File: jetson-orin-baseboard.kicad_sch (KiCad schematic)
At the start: 4 parts

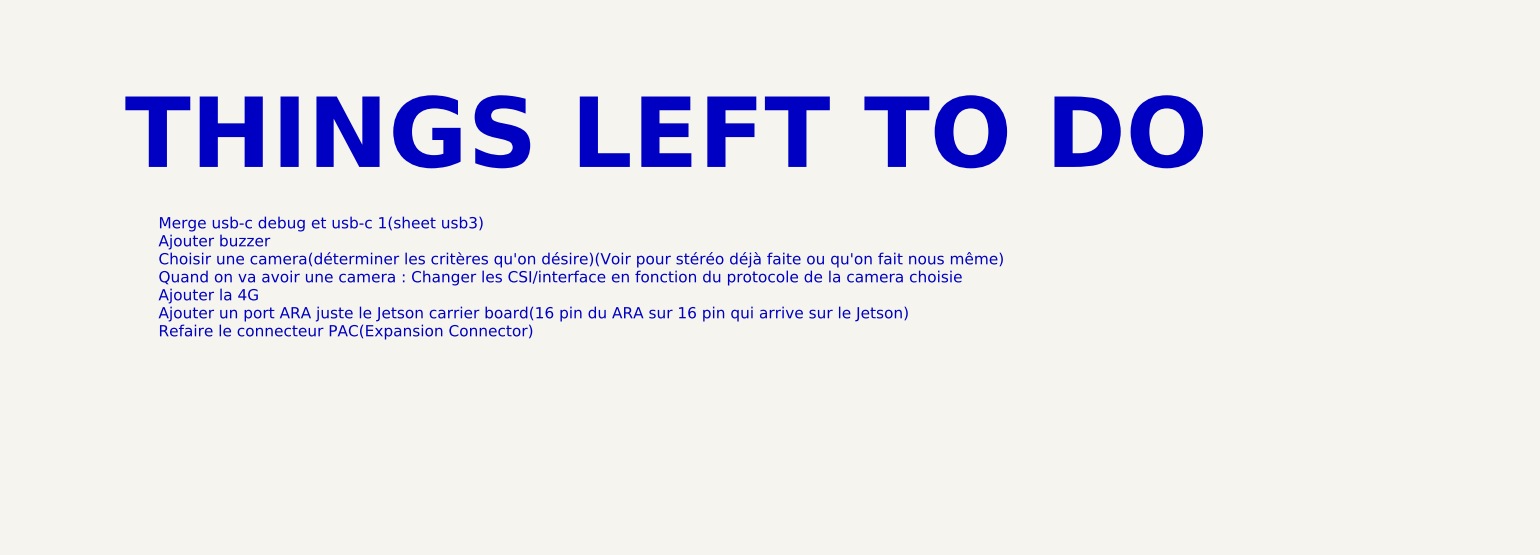
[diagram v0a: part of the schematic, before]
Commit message: Buzzer ajouté
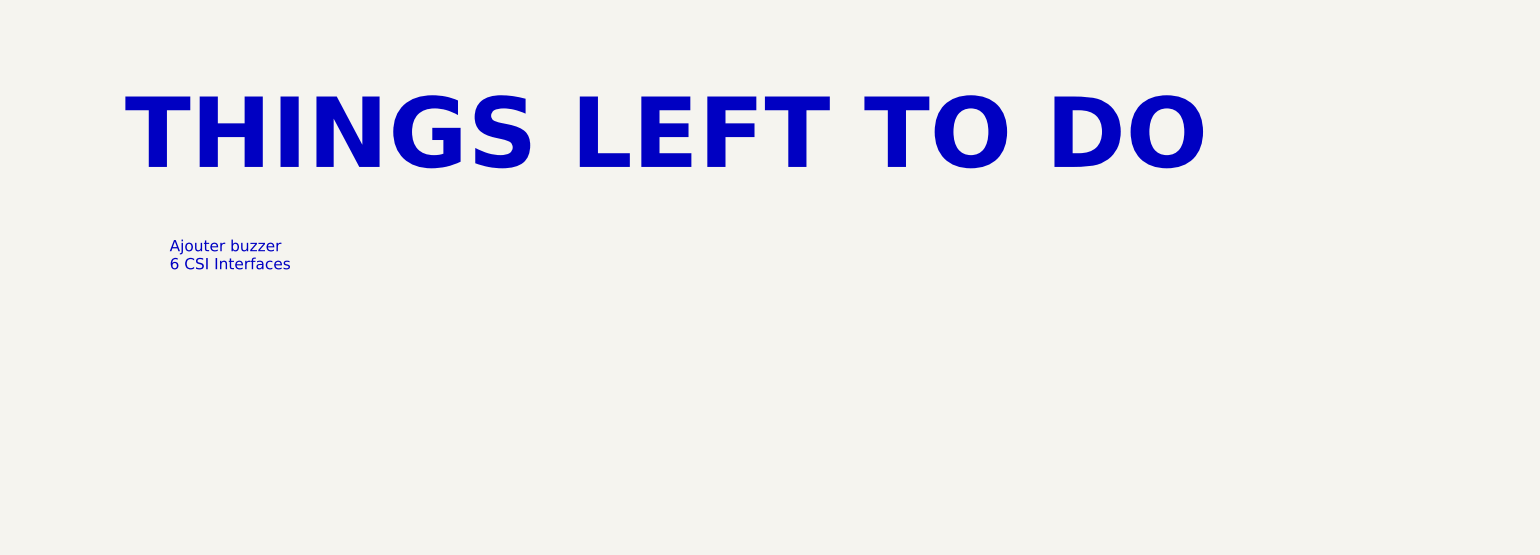
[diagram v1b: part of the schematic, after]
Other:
- note added: "Ajouter buzzer 6 CSI Interfaces"
- note removed: "Merge usb-c debug et usb-c 1(sheet usb3) Ajouter buzzer Choisir une camera(déterminer les critères qu'on désire)(Voir pour stéréo déjà faite ou qu'on fait nous même) Quand on va avoir une camera : Changer les CSI/interface en fonction du protocole de la camera choisie Ajouter la 4G Ajouter un port ARA juste le Jetson carrier board(16 pin du ARA sur 16 pin qui arrive sur le Jetson) Refaire le conn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"
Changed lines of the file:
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@@
     (effects (font (size 8 8) (thickness 0.3) bold) (justify left bottom))
   )
-  (text "Merge usb-c debug et usb-c 1(sheet usb3)\nAjouter buzzer\nChoisir une camera(déterminer les critères qu'on désire)(Voir pour stéréo déjà faite ou qu'on fait nous même)\nQuand on va avoir une camera : Changer les CSI/interface en fonction du protocole de la camera choisie\nAjouter la 4G\nAjouter un port ARA juste le Jetson carrier board(16 pin du ARA sur 16 pin qui arrive sur le Jetson)\nRefaire le connecteur PAC(Expansion Connector)"
-    (at 155.575 64.135 0)
+  (text "Ajouter buzzer\n6 CSI Interfaces" (at 156.845 56.515 0)
     (effects (font (size 1.27 1.27)) (justify left bottom))
   )

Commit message: Updated list of things to do
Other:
- note added: "6 CSI Interfaces"
- note removed: "Ajouter buzzer 6 CSI Interfaces"
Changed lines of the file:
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@@
     (effects (font (size 8 8) (thickness 0.3) bold) (justify left bottom))
   )
-  (text "Ajouter buzzer\n6 CSI Interfaces" (at 156.845 56.515 0)
+  (text "6 CSI Interfaces" (at 156.845 56.515 0)
     (effects (font (size 1.27 1.27)) (justify left bottom))
   )

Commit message: Little change
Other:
- note removed: "6 CSI Interfaces"
- note removed: "THINGS LEFT TO DO"
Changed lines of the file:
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@@
     (effects (font (size 3 3) (thickness 0.4) bold) (justify left bottom))
-  )
-  (text "THINGS LEFT TO DO" (at 151.765 45.72 0)
-    (effects (font (size 8 8) (thickness 0.3) bold) (justify left bottom))
-  )
-  (text "6 CSI Interfaces" (at 156.845 56.515 0)
-    (effects (font (size 1.27 1.27)) (justify left bottom))
   )
   (text "Jetson Orin Baseboard" (at 13.97 24.765 0)

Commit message: changement vers gmsl2 en cours
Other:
- sheet CSI renamed Cameras
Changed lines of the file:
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@@
     (stroke (width 0.1524) (type solid))
     (fill (color 0 0 0 0.0000))
-    (property "Sheetname" "CSI" (at 171.958 206.2984 0)
+    (property "Sheetname" "Cameras" (at 171.958 206.2984 0)
       (effects (font (size 1.27 1.27)) (justify left bottom))
     )

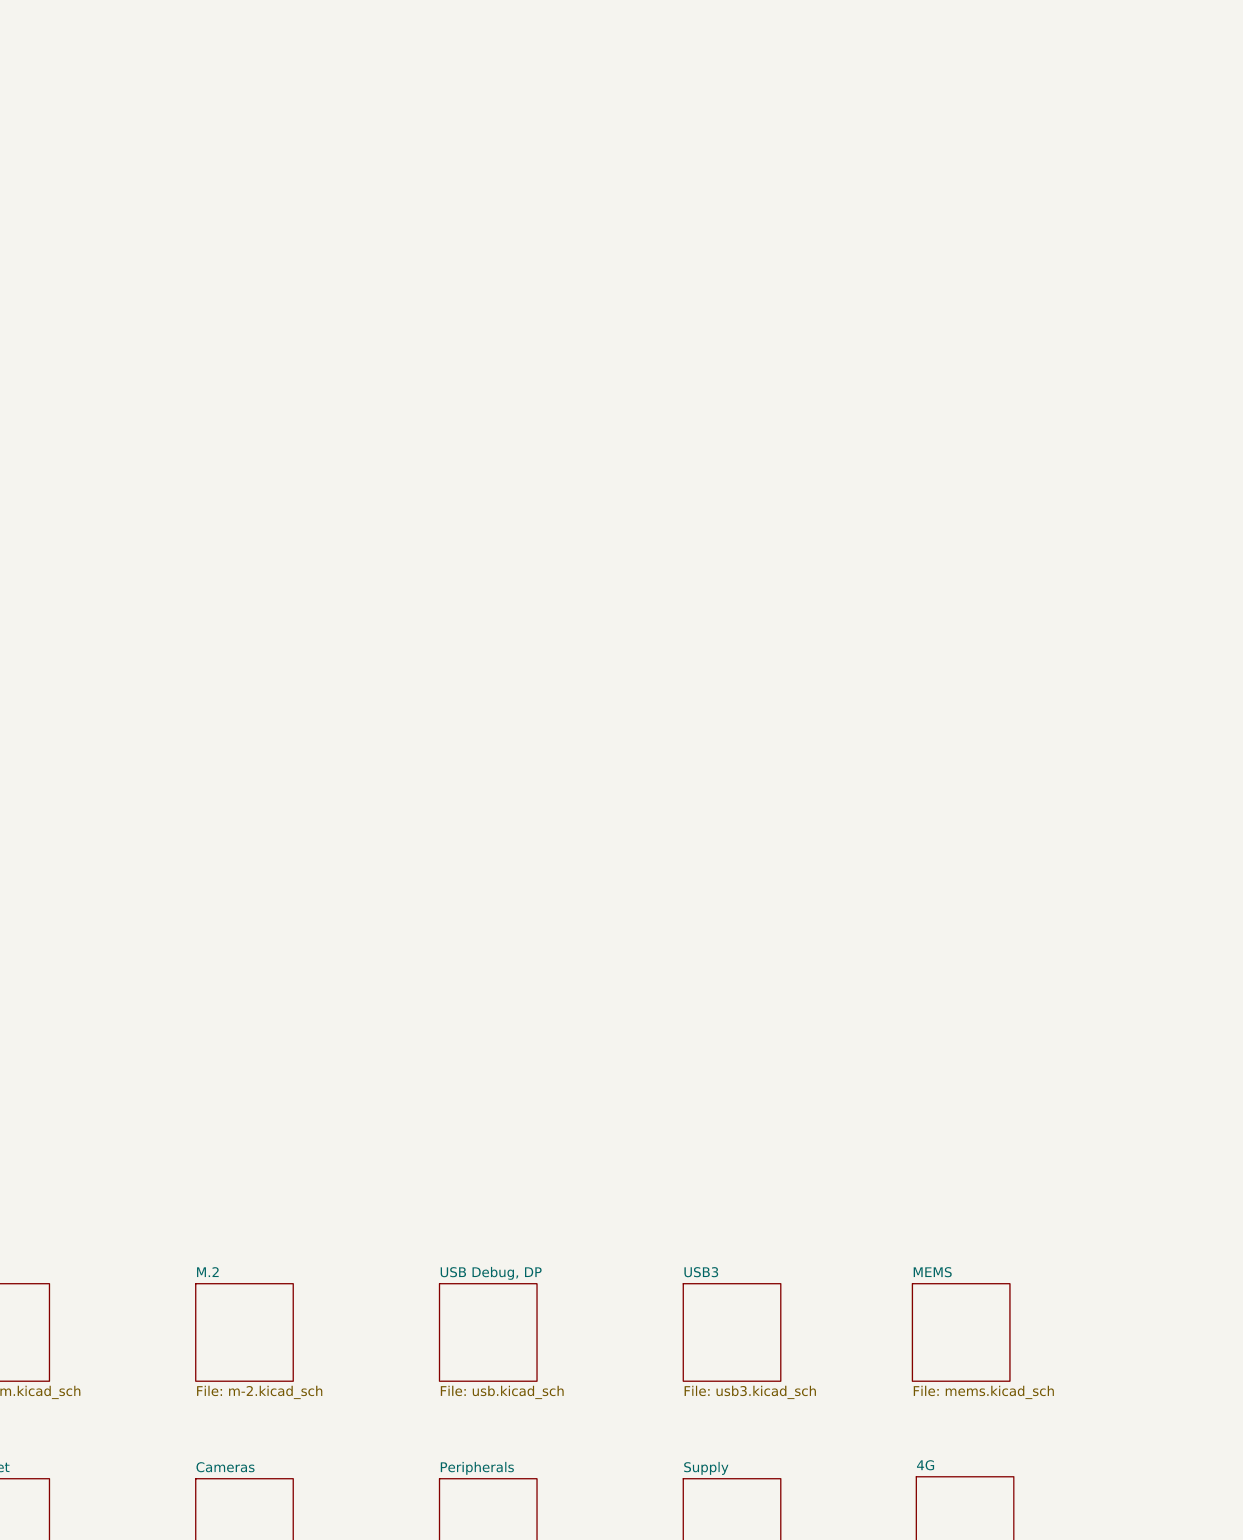
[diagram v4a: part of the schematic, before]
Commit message: Schematic check
Include Pinmux and Schematic Check excels in doc folder and doing a lot of checking and correcting things.
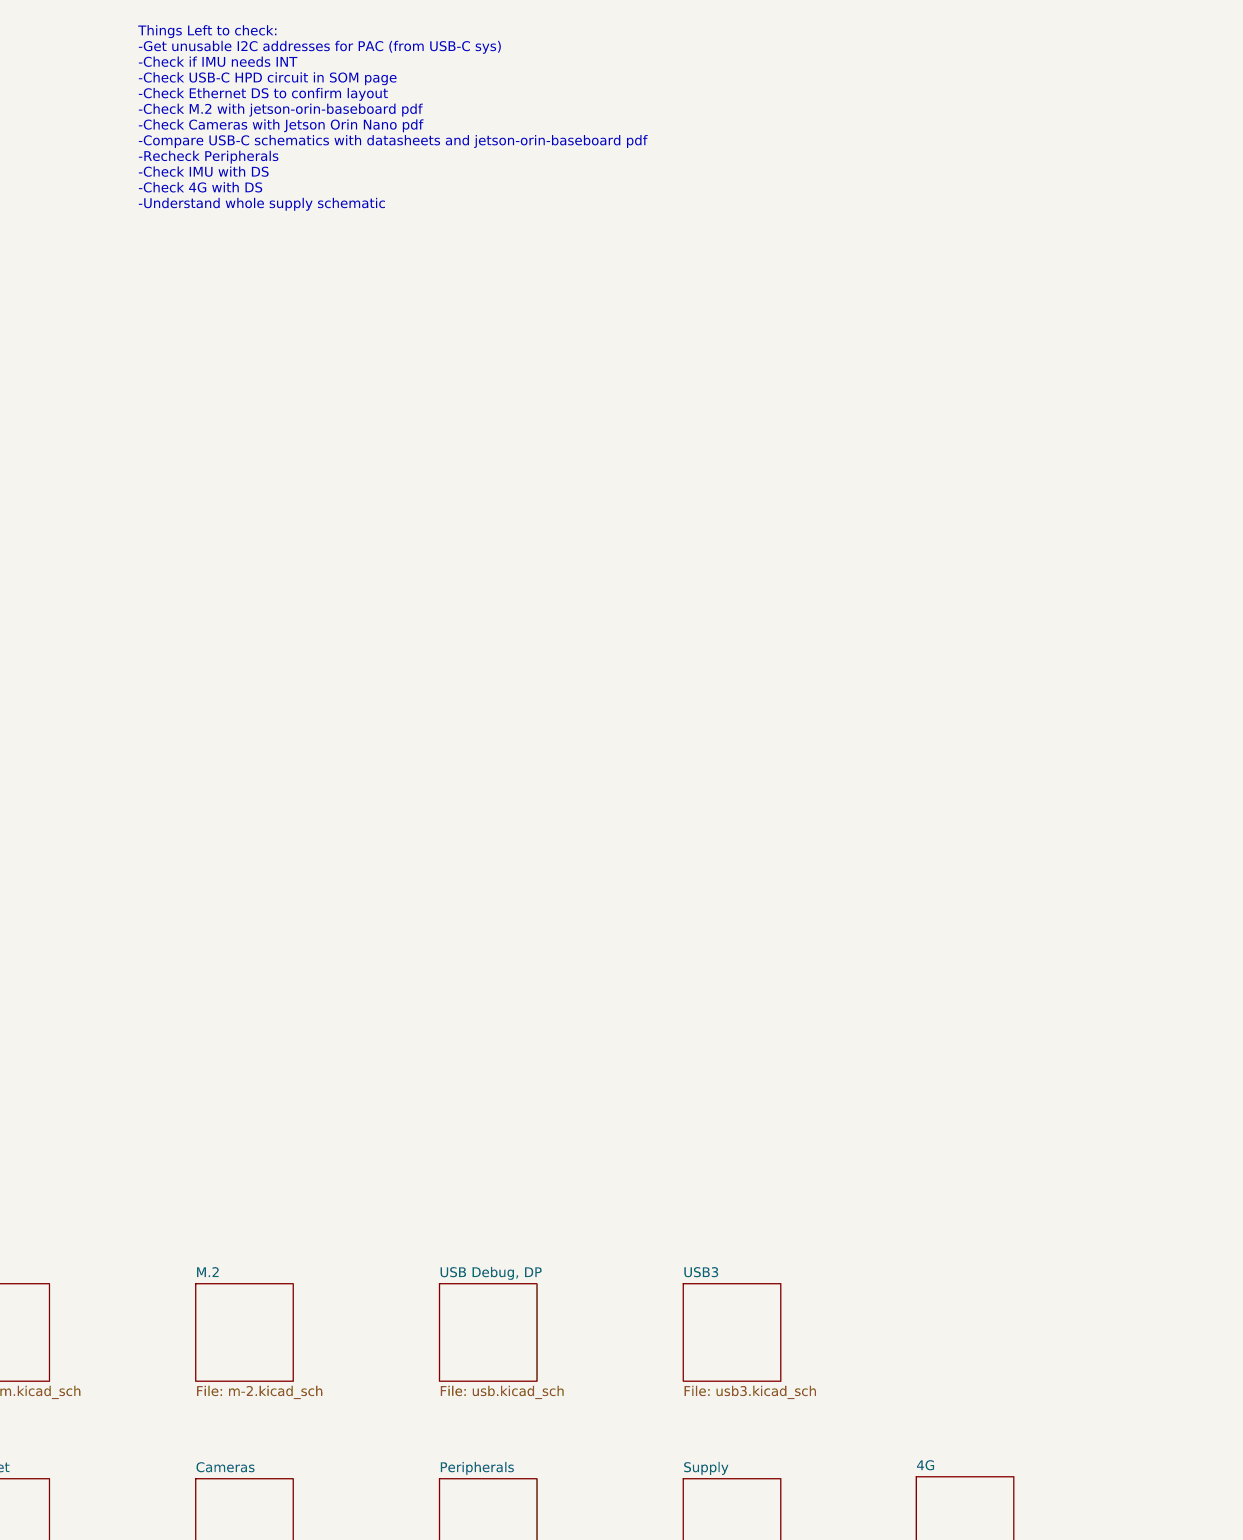
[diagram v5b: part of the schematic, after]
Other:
- removed sheet MEMS
- note added: "Things Left to check: -Get unusable I2C addresses for PAC (from USB-C sys) -Check if IMU needs INT -Check USB-C HPD circuit in SOM page -Check Ethernet DS to confirm layout -Check M.2 with jetson-orin-baseboard pdf -Check Cameras with Jetson Orin Nano pdf -Compare USB-C schematics with datasheets and jetson-orin-baseboard pdf -Recheck Peripherals -Check IMU with DS -Check 4G with DS -Understand w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"
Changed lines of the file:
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@@
     (effects (font (size 5 5) (thickness 0.4) bold) (justify left bottom))
+  )
+  (text "Things Left to check:\n-Get unusable I2C addresses for PAC (from USB-C sys)\n-Check if IMU needs INT\n-Check USB-C HPD circuit in SOM page\n-Check Ethernet DS to confirm layout\n-Check M.2 with jetson-orin-baseboard pdf\n-Check Cameras with Jetson Orin Nano pdf\n-Compare USB-C schematics with datasheets and jetson-orin-baseboard pdf\n-Recheck Peripherals\n-Check IMU with DS\n-Check 4G with DS\n-Understand whole supply schematic"
+    (at 164.465 41.91 0)
+    (effects (font (size 1.27 1.27)) (justify left bottom))
   )
   (symbol (lib_id "jetson-orin-baseboard:GND") (at 383.54 246.38 0) (unit 1)
@@
       )
     )
-  )
-  (sheet (at 265.303 181.61) (size 12.7 12.7) (fields_autoplaced)
-    (stroke (width 0.1524) (type solid))
-    (fill (color 0 0 0 0.0000))
-    (property "Sheetname" "MEMS" (at 265.303 180.8984 0)
-      (effects (font (size 1.27 1.27)) (justify left bottom))
-    )
-    (property "Sheetfile" "mems.kicad_sch" (at 265.303 194.8946 0)
-      (effects (font (size 1.27 1.27)) (justify left top))
-    )
-    (instances
-      (project "jetson-orin-baseboard"
-        (path "/4b393452-b11e-416e-bc83-918ae3cab2f1" (page "10"))
-      )
-    )

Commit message: Small changes
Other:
- note added: "Things Left to check: -Check USB-C HPD circuit in SOM page -Check Ethernet DS to confirm layout -Compare USB-C schematics with datasheets and jetson-orin-baseboard pdf -Recheck Peripherals -Check IMU with DS -Check 4G with DS -Understand whole supply schematic"
- note removed: "Things Left to check: -Get unusable I2C addresses for PAC (from USB-C sys) -Check if IMU needs INT -Check USB-C HPD circuit in SOM page -Check Ethernet DS to confirm layout -Check M.2 with jetson-orin-baseboard pdf -Check Cameras with Jetson Orin Nano pdf -Compare USB-C schematics with datasheets and jetson-orin-baseboard pdf -Recheck Peripherals -Check IMU with DS -Check 4G with DS -Understand w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"
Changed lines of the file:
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@@
     (effects (font (size 5 5) (thickness 0.4) bold) (justify left bottom))
   )
-  (text "Things Left to check:\n-Get unusable I2C addresses for PAC (from USB-C sys)\n-Check if IMU needs INT\n-Check USB-C HPD circuit in SOM page\n-Check Ethernet DS to confirm layout\n-Check M.2 with jetson-orin-baseboard pdf\n-Check Cameras with Jetson Orin Nano pdf\n-Compare USB-C schematics with datasheets and jetson-orin-baseboard pdf\n-Recheck Peripherals\n-Check IMU with DS\n-Check 4G with DS\n-Understand whole supply schematic"
+  (text "Things Left to check:\n-Check USB-C HPD circuit in SOM page\n-Check Ethernet DS to confirm layout\n-Compare USB-C schematics with datasheets and jetson-orin-baseboard pdf\n-Recheck Peripherals\n-Check IMU with DS\n-Check 4G with DS\n-Understand whole supply schematic"
     (at 164.465 41.91 0)
     (effects (font (size 1.27 1.27)) (justify left bottom))
